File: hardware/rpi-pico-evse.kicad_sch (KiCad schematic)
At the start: 33 parts, among them J1 Power, J2 Power Relays, J3 Pilot, Q1 IRLB8721PBF, Q2 IRLB8721PBF, SW1 KY-040, U1 L7805, U2 Pico, U3 6N138, U4 LM339

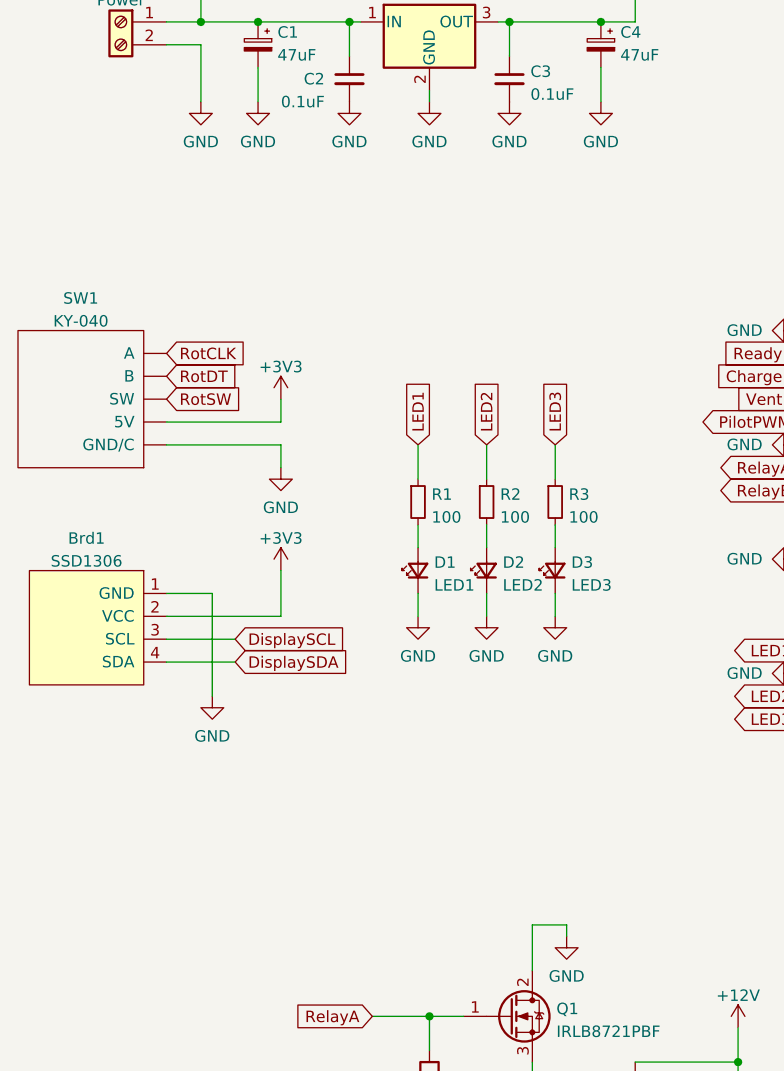
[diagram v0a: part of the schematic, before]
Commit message: Singular rotary and rotation debounce.
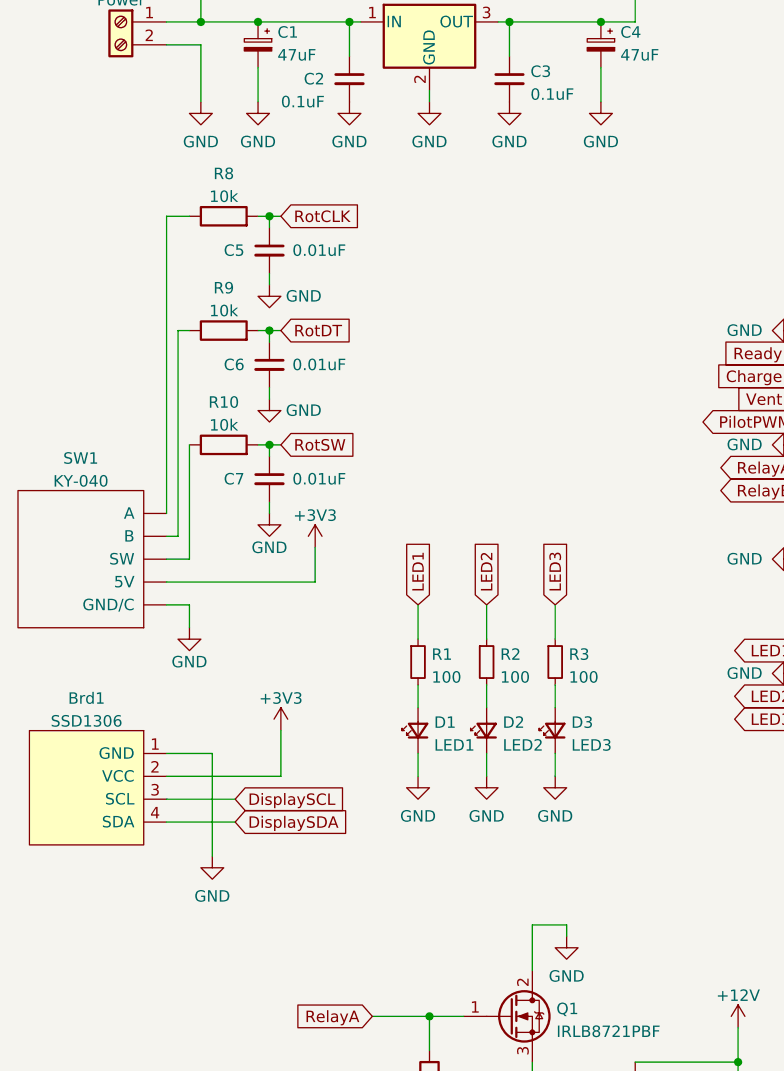
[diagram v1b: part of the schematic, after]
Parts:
- added C5, C6, C7: 0.01uF, symbol Device:C_Small
- added R10, R8, R9: 10k, symbol Device:R
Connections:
- net GND: now also C5.2, C6.2, C7.2
- net RotCLK: now also C5.1, R8.2; no longer SW1.~ (SW)
- net RotDT: now also C6.1, R9.2; no longer SW1.~ (SW)
- net RotSW: now also C7.1, R10.2; no longer SW1.~ (SW)
- new net: R8.1, SW1.~ (SW)
- new net: R9.1, SW1.~ (SW)
- new net: R10.1, SW1.~ (SW)
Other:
- moved on the sheet: Brd1, D1, D2, D3, R1, R2, R3, SW1
